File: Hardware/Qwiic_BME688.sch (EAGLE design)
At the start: 30 parts, among them J2 QWIIC_RA, J4 QWIIC_RA, U1 BME688LGA

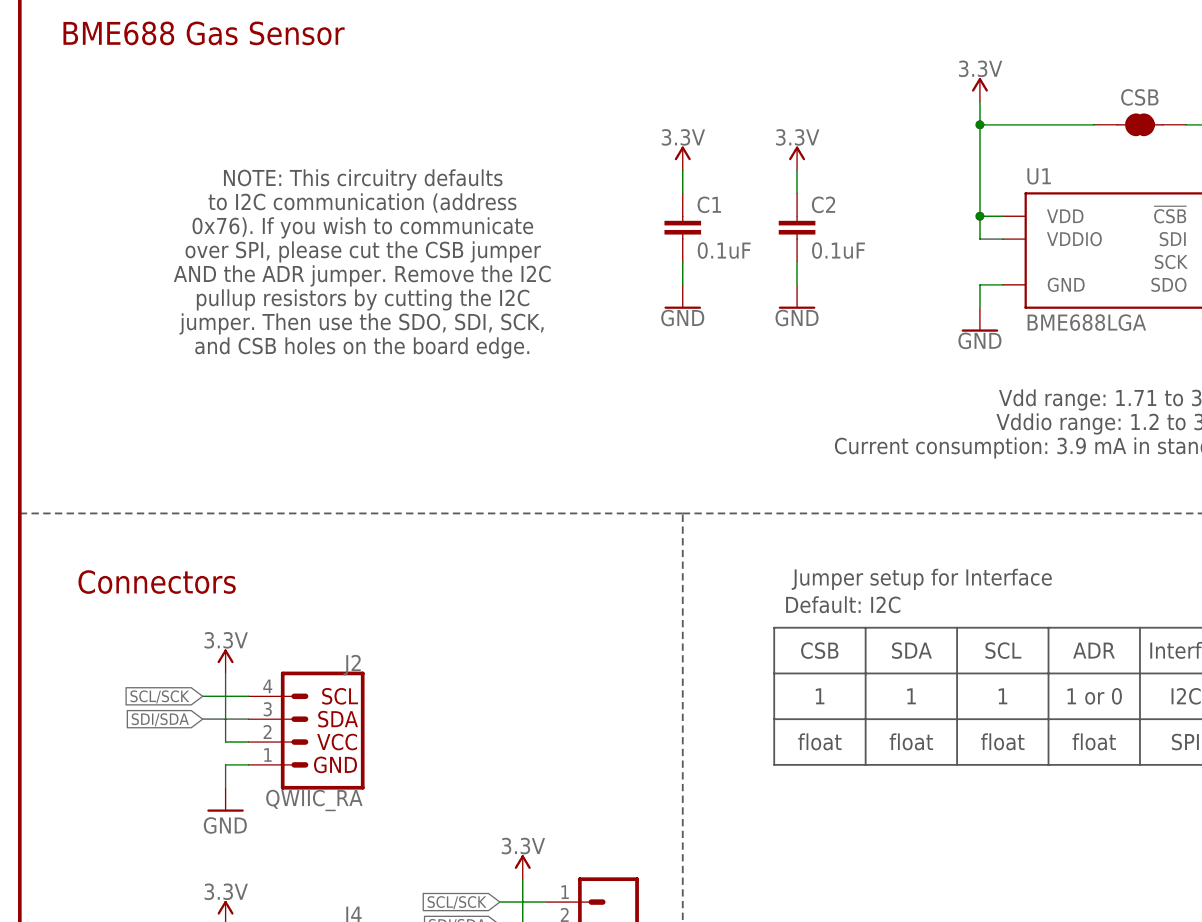
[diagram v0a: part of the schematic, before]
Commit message: Change I2C jumper notes on schematic
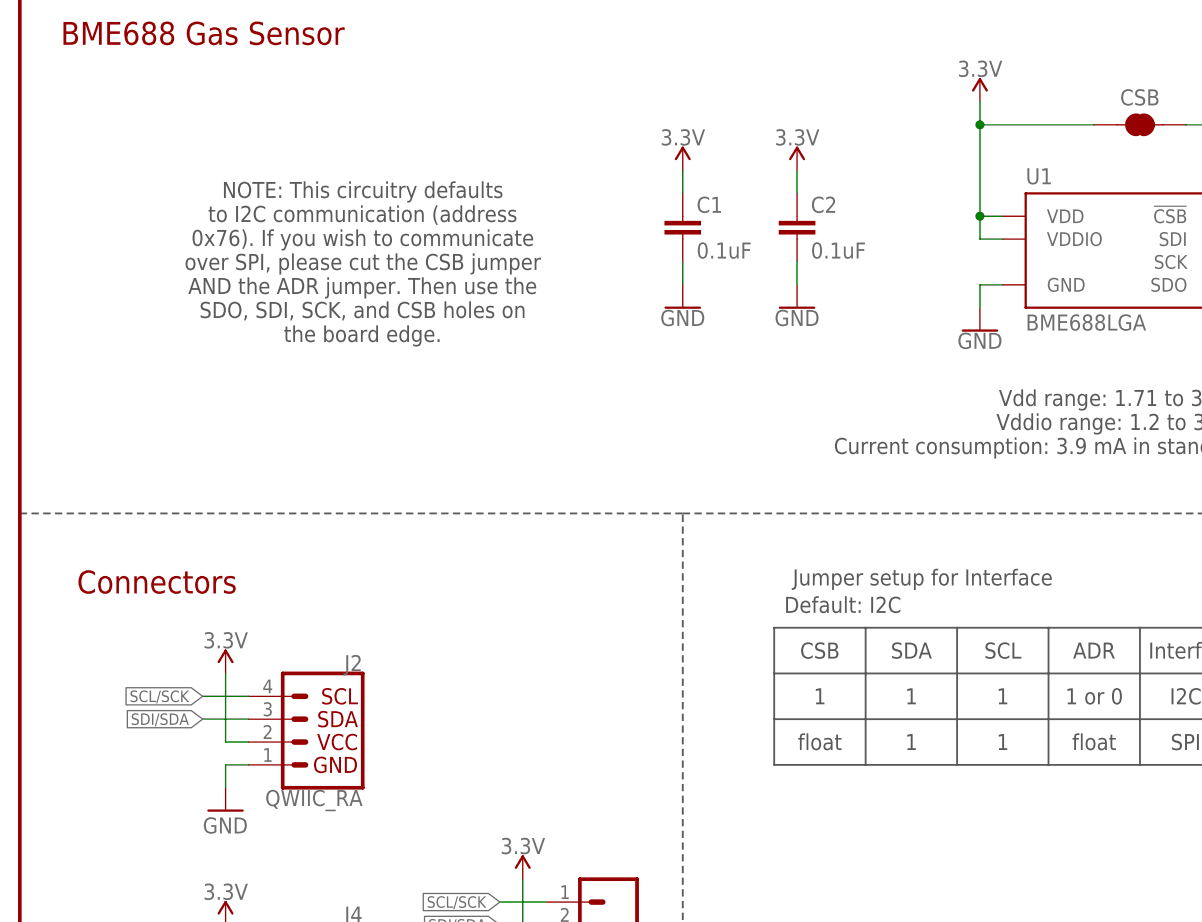
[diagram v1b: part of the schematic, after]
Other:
- note added: "NOTE: This circuitry defaults to I2C communication (address 0x76). If you wish to communicate over SPI, please cut the CSB jumper AND the ADR jumper. Then use the SDO, SDI, SCK, and CSB holes on the board edge."
- note removed: "NOTE: This circuitry defaults to I2C communication (address 0x76). If you wish to communicate over SPI, please cut the CSB jumper AND the ADR jumper. Remove the I2C pullup resistors by cutting the I2C jumper. Then use the SDO, SDI, SCK, and CSB holes on the board edge."
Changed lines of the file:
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@@
 0x76). If you wish to communicate
 over SPI, please cut the CSB jumper
-AND the ADR jumper. Remove the I2C
-pullup resistors by cutting the I2C
-jumper. Then use the SDO, SDI, SCK,
-and CSB holes on the board edge.</text>
+AND the ADR jumper. Then use the
+SDO, SDI, SCK, and CSB holes on
+the board edge.</text>
 <text x="109.22" y="53.34" size="1.778" layer="97" font="vector" align="center">SCL</text>
 <text x="88.9" y="53.34" size="1.778" layer="97" font="vector" align="center">CSB</text>
@@
 <text x="119.38" y="48.26" size="1.778" layer="97" font="vector" align="center">1 or 0</text>
 <text x="88.9" y="43.18" size="1.778" layer="97" font="vector" align="center">float</text>
-<text x="109.22" y="43.18" size="1.778" layer="97" font="vector" align="center">float</text>
+<text x="109.22" y="43.18" size="1.778" layer="97" font="vector" align="center">1</text>
 <text x="119.38" y="43.18" size="1.778" layer="97" font="vector" align="center">float</text>
 <text x="130.302" y="53.34" size="1.778" layer="97" font="vector" align="center">Interface</text>
@@
 <text x="99.06" y="53.34" size="1.778" layer="97" font="vector" align="center">SDA</text>
 <text x="99.06" y="48.26" size="1.778" layer="97" font="vector" align="center">1</text>
-<text x="99.06" y="43.18" size="1.778" layer="97" font="vector" align="center">float</text>
+<text x="99.06" y="43.18" size="1.778" layer="97" font="vector" align="center">1</text>
 <text x="100.33" y="61.468" size="1.778" layer="97" font="vector" align="center">Jumper setup for Interface</text>
 <text x="91.44" y="58.42" size="1.778" layer="97" font="vector" align="center">Default: I2C</text>
